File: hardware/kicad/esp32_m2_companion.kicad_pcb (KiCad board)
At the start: 4 copper layers, 22 x 42 mm, 32 parts, among them J1 M2_KEYB_2242_EDGE, J3 Conn_01x12, U1 USBLC6-2SC6, U2 ESP32-S3-WROOM-1

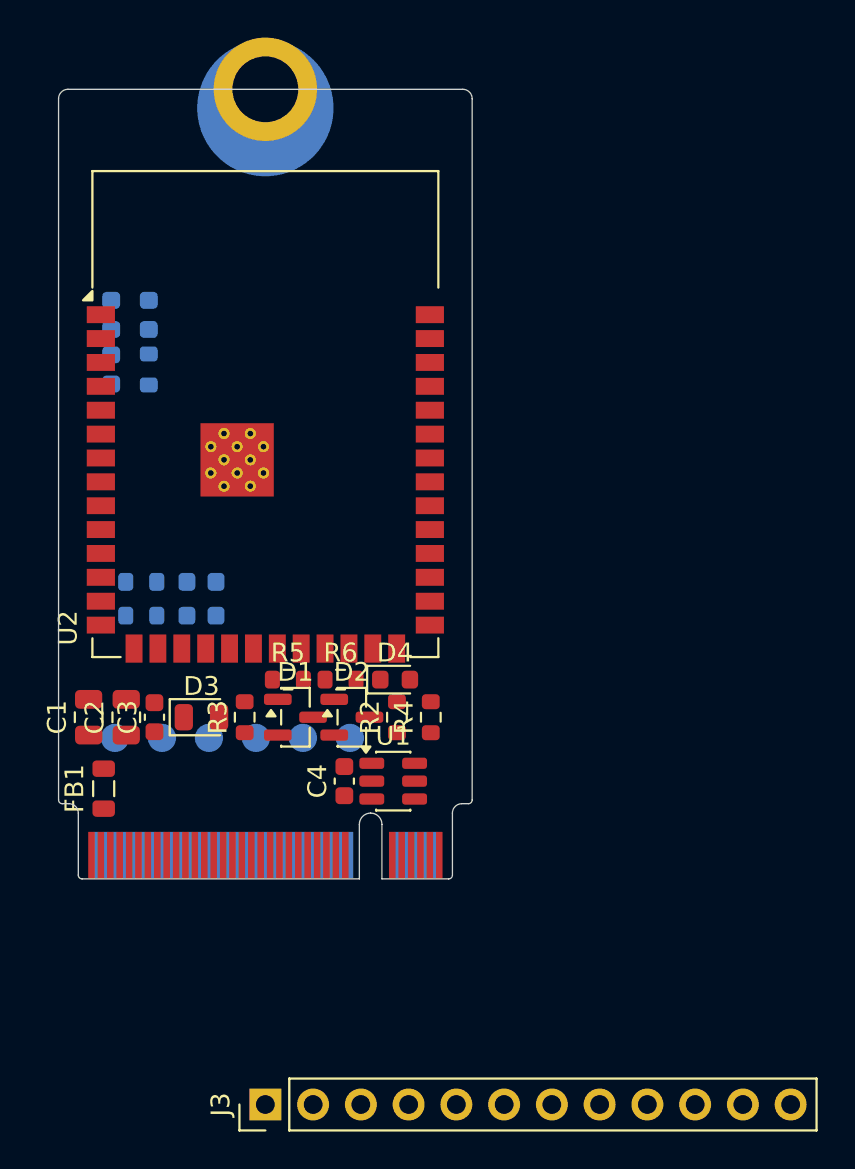
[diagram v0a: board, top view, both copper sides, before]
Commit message: ADR 0005: JST SH connectors (Qwiic + SH-8) replace 2.54 header; top/bottom re-split; 3D outputs
- io_header: J3=SM04B-SRSS-TB (C160404) Qwiic, J4=SM08B-SRSS-TB (C160407)
- top = module + connectors; bottom = passives/ESD/LEDs/TPs (connector
  courtyards consume the lower top zone - documented in layout-notes)
- R11: M.2 height envelope violation (module 3.1mm) accepted for open slots
- DRC: no shorts/clearance errors; GLB export + raytraced renders
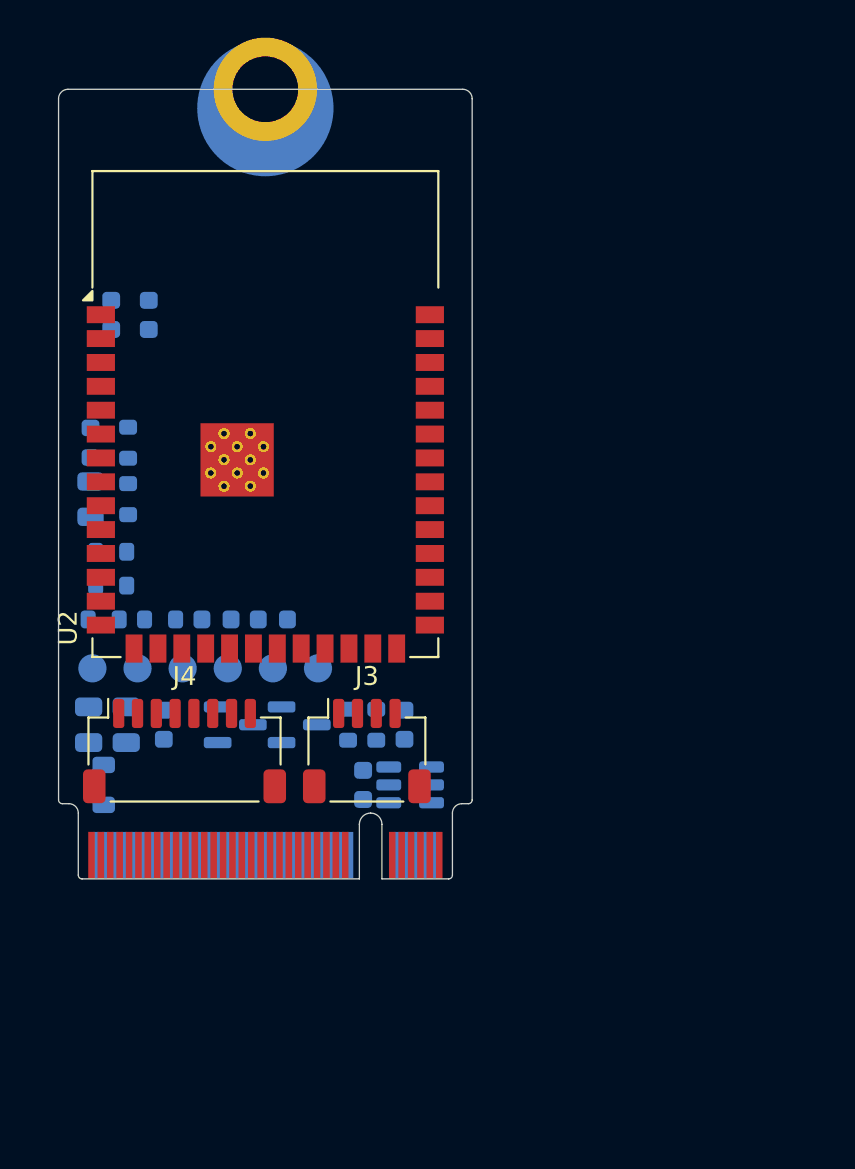
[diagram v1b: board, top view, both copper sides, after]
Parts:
- added J4: Conn_01x08, Connector_JST:JST_SH_SM08B-SRSS-TB_1x08-1MP_P1.00mm_Horizontal, F.Cu at (95.7, 143.2)
- C1, C2, C3, C4, D1, D2, D3, D4, FB1, R2, R3, R4, R5, R6, U1: moved to B.Cu
- J3: value Conn_01x12 -> Conn_01x04; footprint Connector_PinHeader_2.54mm:PinHeader_1x12_P2.54mm_Vertical -> Connector_JST:JST_SH_SM04B-SRSS-TB_1x04-1MP_P1.00mm_Horizontal
- moved C5 24.5 mm to (107.4, 141.8)
- moved R1 22.4 mm to (105.9, 141.8)
- moved R4 21.7 mm to (92.7, 126.8)
- moved D4 20.5 mm to (90.7, 126.8), turned to 90 degrees
- moved J3 19.6 mm to (105.4, 143.2), turned to 0 degrees
- moved R3 13.2 mm to (92.7, 129.8)
- moved D3 13.0 mm to (90.7, 129.8), turned to 90 degrees
- moved R5 10.3 mm to (91.4, 136.2)
- moved R6 10.1 mm to (94.4, 136.2)
- moved C9 4.29 mm to (100.4, 136.2)
- moved TP6 4.07 mm to (102.8, 138.8)
- moved TP5 4.03 mm to (100.4, 138.8)
- moved TP4 3.99 mm to (98.0, 138.8)
- moved TP3 3.96 mm to (95.6, 138.8)
- moved TP2 3.92 mm to (93.2, 138.8)
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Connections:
- J3 pad 1: +3V3 -> GND
- J3 pad 2: GND -> +3V3

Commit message: ADR 0005 amendment: vertical JST SH (BM04B/BM08B) — side-entry unmatable in-slot
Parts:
- J3: footprint Connector_JST:JST_SH_SM04B-SRSS-TB_1x04-1MP_P1.00mm_Horizontal -> Connector_JST:JST_SH_BM04B-SRSS-TB_1x04-1MP_P1.00mm_Vertical
- J4: footprint Connector_JST:JST_SH_SM08B-SRSS-TB_1x08-1MP_P1.00mm_Horizontal -> Connector_JST:JST_SH_BM08B-SRSS-TB_1x08-1MP_P1.00mm_Vertical
- moved J3 1.44 mm to (104.2, 144.0)
- moved J4 1.00 mm to (95.1, 144.0)

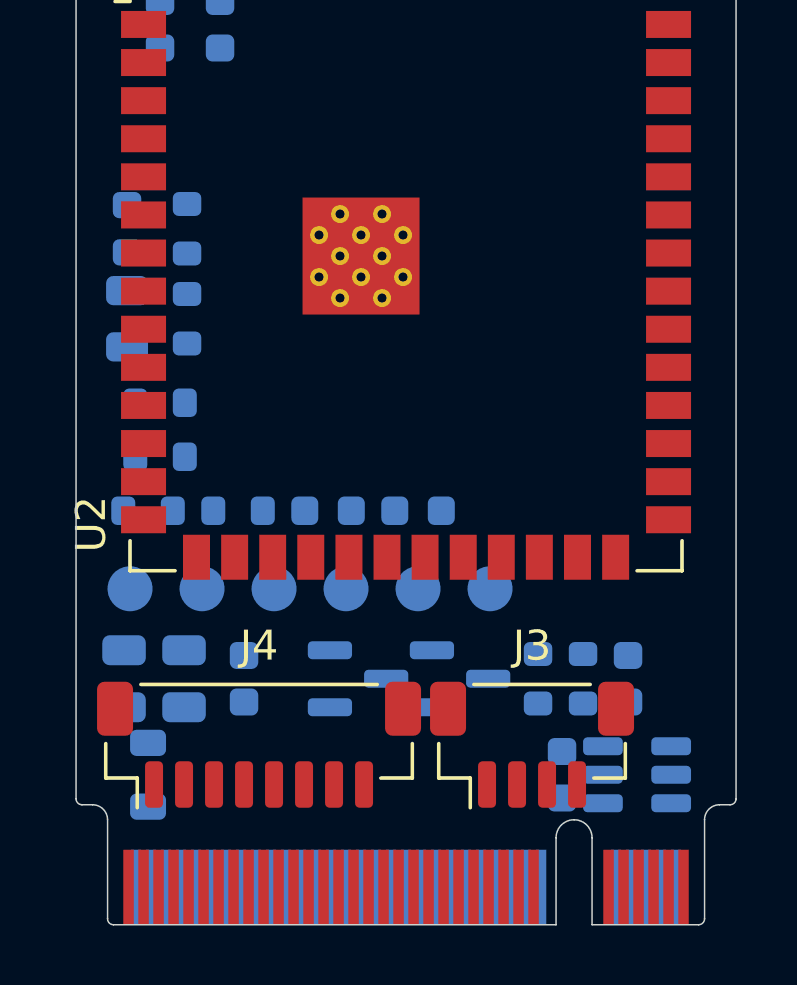
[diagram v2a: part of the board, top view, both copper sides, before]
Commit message: Socket-zone fix (owner-caught) + datasheet mechanical/product views
- EM spec Figs 38/39: mated socket covers first 4.8mm of card both faces;
  U1/C4/FB1/J3/J4 were inside it — re-placed, courtyard added to edge
  footprint so DRC enforces the zone permanently
- JST eSH catalog stored: BM header 4.2mm tall (~6.3 mated) = card max height
- gen_views.py: Mallow-style labeled top/bottom views + dimensioned
  mechanical drawing, callout legends shared with gen_datasheet
- DATASHEET.md: product views + mechanical data sections, corrected heights
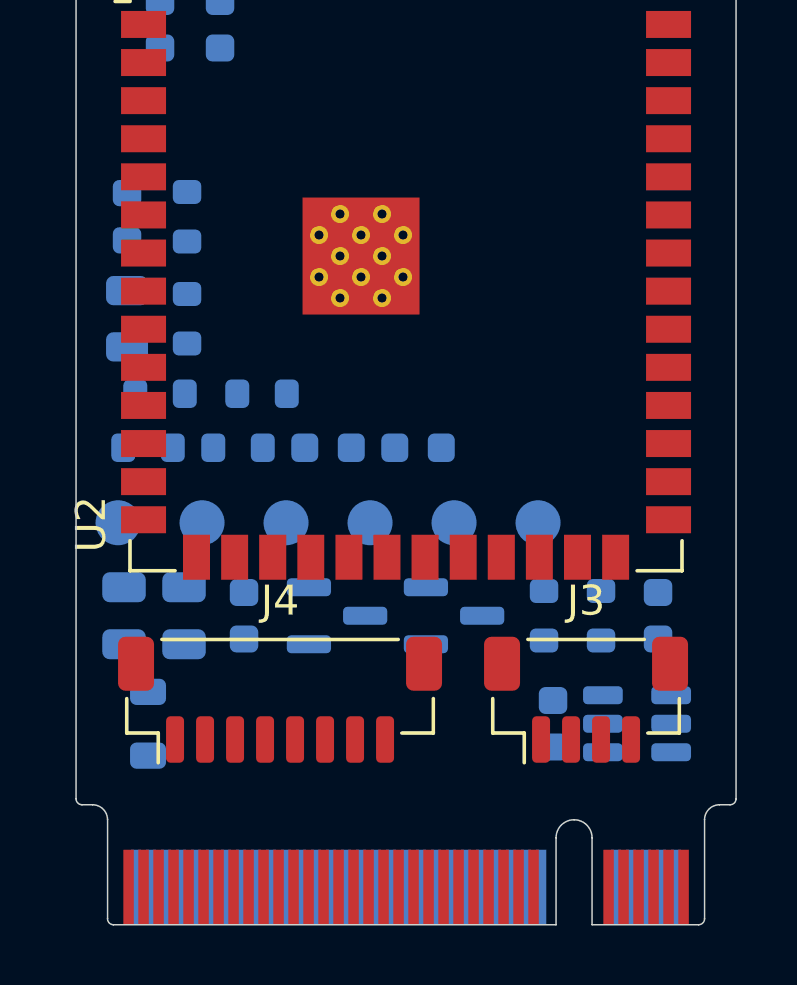
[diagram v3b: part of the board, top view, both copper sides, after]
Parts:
- moved R8 3.41 mm to (95.2, 132.3)
- moved TP6 2.72 mm to (104.4, 136.6)
- moved TP5 2.51 mm to (101.6, 136.6)
- moved J3 2.34 mm to (106.0, 142.5)
- moved TP4 2.34 mm to (98.8, 136.6)
- moved C5 2.33 mm to (108.4, 139.7)
- moved TP3 2.24 mm to (96.0, 136.6)
- moved TP1 2.24 mm to (90.4, 136.6)
- moved D1 2.21 mm to (97.7, 139.7)
- moved TP2 2.20 mm to (93.2, 136.6)
- moved R1 2.18 mm to (106.5, 139.7)
- moved D2 2.11 mm to (101.6, 139.7)
- moved R2 2.11 mm to (104.6, 139.7)
- moved C1 2.10 mm to (90.6, 139.7)
- moved C2 2.10 mm to (92.6, 139.7)
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
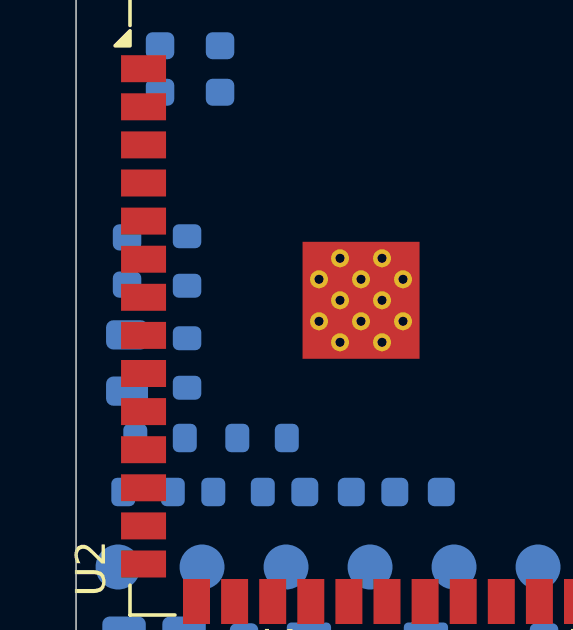
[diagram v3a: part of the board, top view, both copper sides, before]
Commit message: Side-view LEDs at left card edge (owner-caught: top-emitting invisible in-slot)
- D3/D4 -> TOGIALED TJ-S1706SW6T side-view (C273616/C273612), 330R series
- corrected wrong orientation claim in layout-notes (card top faces AWAY
  from host; bottom faces host at ~2.5mm)
- ADR 0003 amended; datasheet/views regenerated
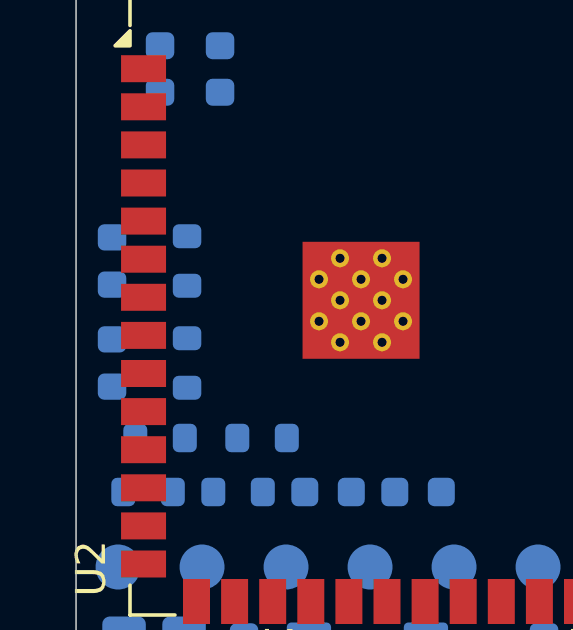
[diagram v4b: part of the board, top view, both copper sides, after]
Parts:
- D3: footprint LED_SMD:LED_0805_2012Metric -> LED_SMD:LED_0603_1608Metric
- R3, R4: value 1k -> 330R
- moved D3 0.50 mm to (90.2, 129.8)
- moved D4 0.50 mm to (90.2, 126.4)

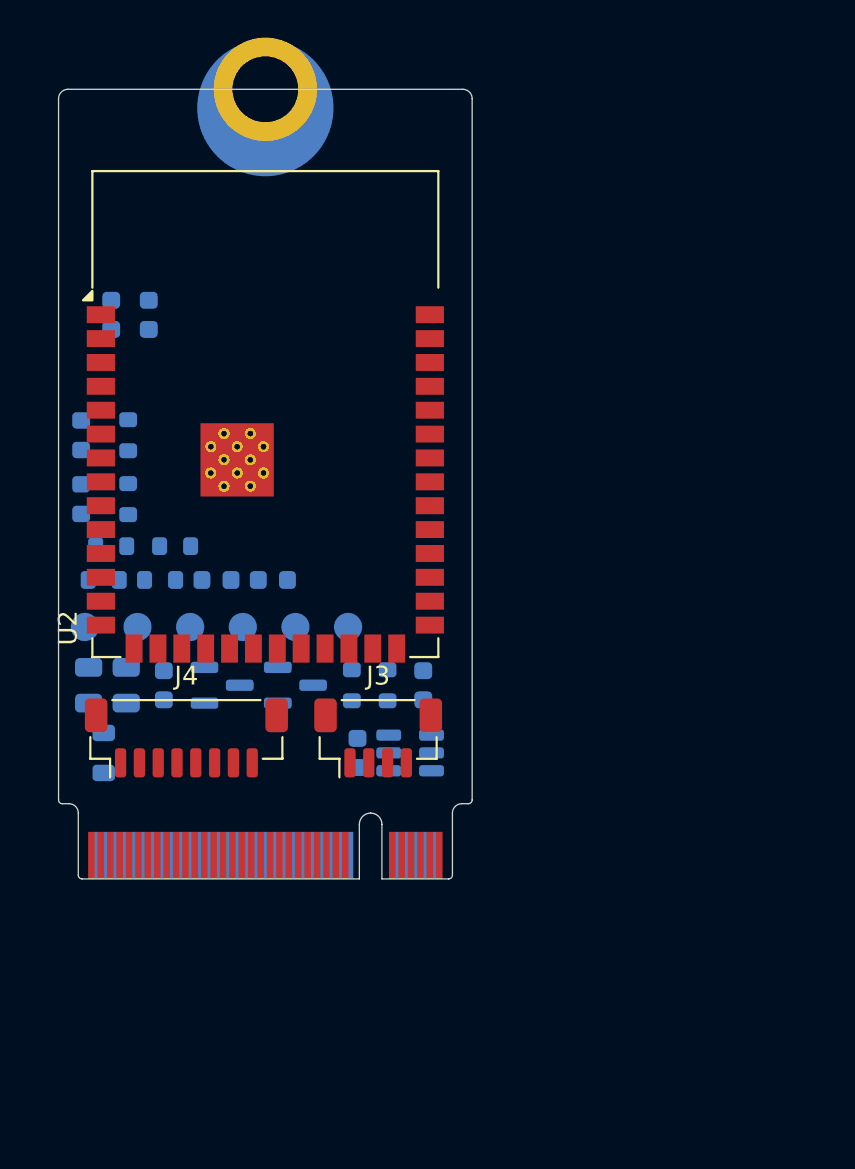
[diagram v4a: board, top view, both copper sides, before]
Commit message: Phase 2 routing: USB diff-pair + planes + 27/28 nets (scripted route.py)
- tools/route.py: hand-routed 90ohm USB pair (0.14/0.14, L2-referenced),
  freerouting for remaining signals, 4 plane pours, EPAD via grid, GND stitch
- 27/28 nets routed & DRC-clean vs JLCPCB minima; 1 net (W_DISABLE1_n,
  secondary BOOT strap) left for interactive finish — see docs/routing-status.md
- USB_DIFF geometry from JLC04081H-3313 stackup (verify at order via impedance tool)
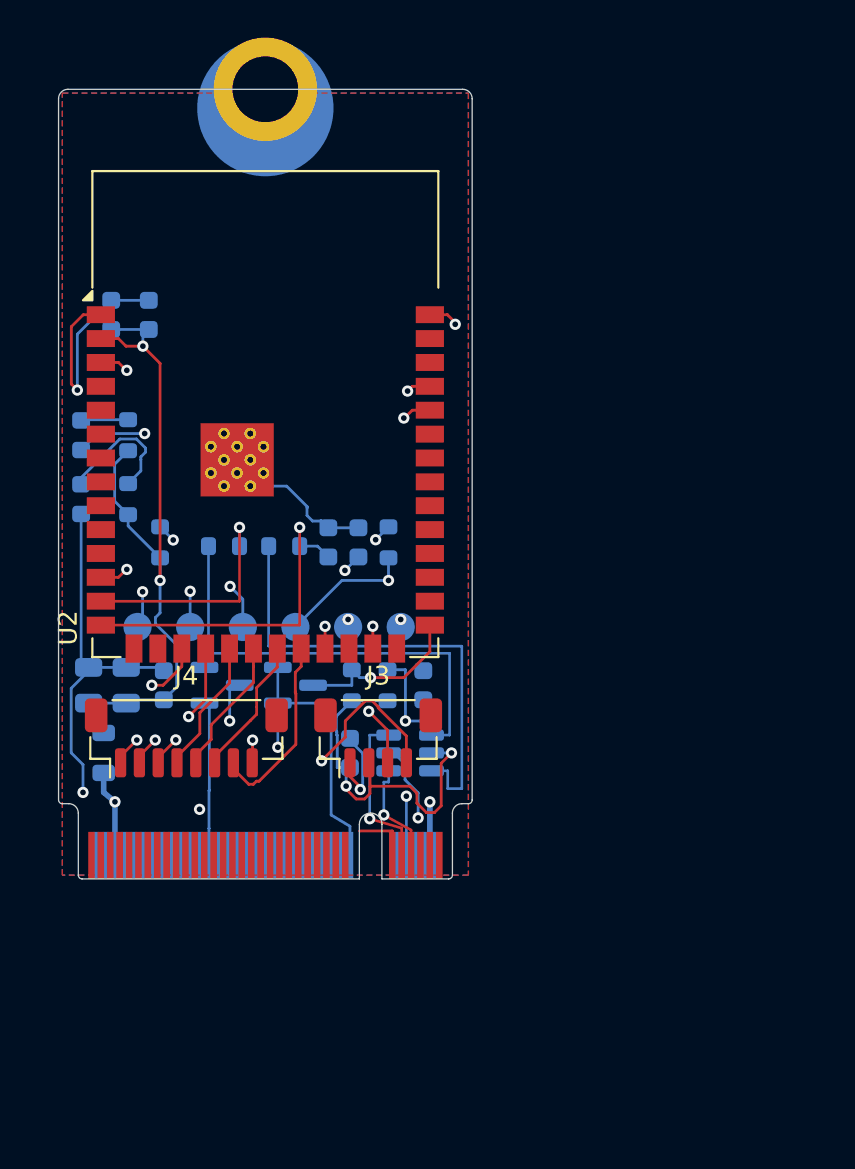
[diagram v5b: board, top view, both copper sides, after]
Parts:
- moved TP1 16.8 mm to (107.2, 136.6)
- moved R5 15.3 mm to (106.5, 132.1), turned to 90 degrees
- moved R7 9.20 mm to (101.0, 132.3)
- moved C8 6.28 mm to (103.3, 132.1), turned to 90 degrees
- moved C9 4.97 mm to (105.0, 132.1), turned to 90 degrees
- moved R8 2.60 mm to (97.8, 132.3)
- moved R6 2.00 mm to (94.4, 132.1), turned to 90 degrees
- moved C4 0.40 mm to (104.5, 143.3)
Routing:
- net GND: track 0.00 -> 138.3 mm, vias 0 -> 19
- net +3V3: track 0.00 -> 89.4 mm, vias 0 -> 5
- net EN: track 0.00 -> 46.5 mm, vias 0 -> 4
- net TXD0: track 0.00 -> 36.3 mm, vias 0 -> 3
- net RXD0: track 0.00 -> 33.5 mm, vias 0 -> 3
- net IO9: track 0.00 -> 31.4 mm, vias 0 -> 3
- net IO8: track 0.00 -> 30.1 mm, vias 0 -> 3
- net LED_STATUS_n: track 0.00 -> 27.9 mm, vias 0 -> 2
- net +3V3_M2: track 0.00 -> 27.4 mm, vias 0 -> 2
- net IO0_BOOT: track 0.00 -> 26.7 mm, vias 0 -> 2
- net USB_D_P_ESD: track 0.00 -> 25.7 mm
- net USB_D_N_ESD: track 0.00 -> 23.8 mm
- net USB_D_N: track 0.00 -> 19.9 mm, vias 0 -> 2
- net USB_D_P: track 0.00 -> 18.5 mm, vias 0 -> 1
- net W_DISABLE1_n: track 0.00 -> 16.8 mm, vias 0 -> 2
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- added copper zone on In2.Cu, net +3V3
- added copper zone on B.Cu, net GND
- added copper zone on F.Cu, net GND
- added copper zone on In1.Cu, net GND
